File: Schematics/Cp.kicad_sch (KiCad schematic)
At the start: 60 parts, among them Q10 J201, Q11 J201, Q3 2SC1815, Q4 2SC1815, Q5 2SC1815, Q6 2SC1815, Q7 2SC1815, Q8 2SC1815, Q9 2SC1815, SW1 SW_SPDT, U1 CA3080

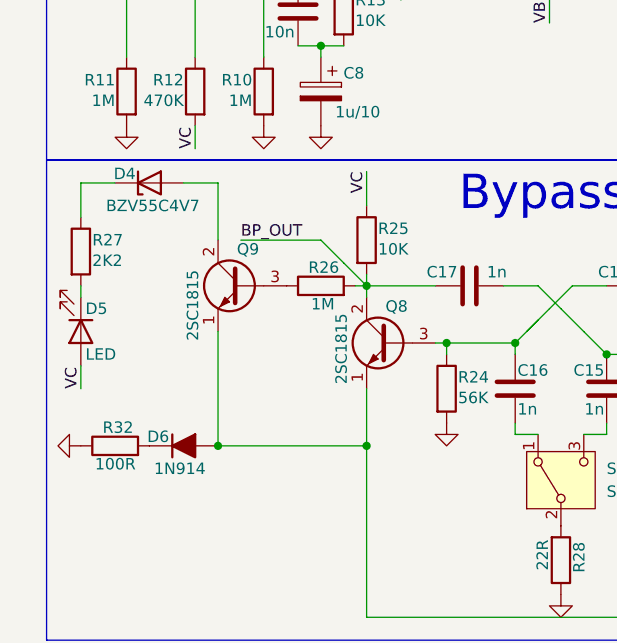
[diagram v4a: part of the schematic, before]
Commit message: Schem upd
The LED is powered by the low voltage supply, not by the effect
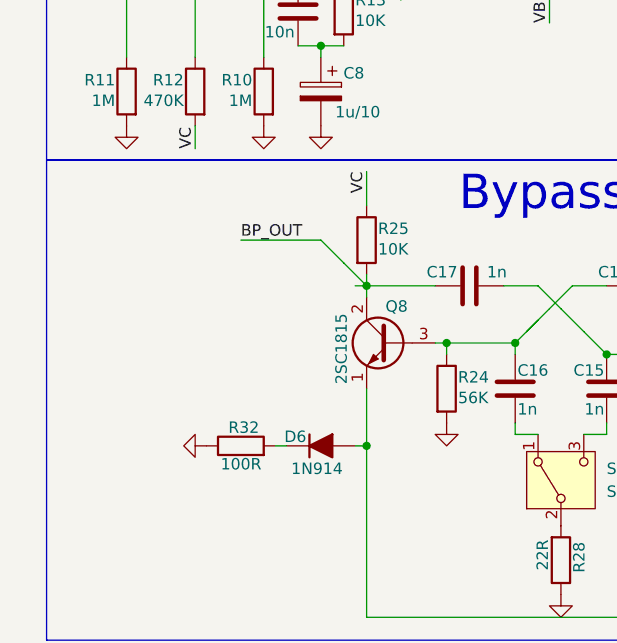
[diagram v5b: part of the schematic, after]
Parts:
- removed D4: BZV55C4V7, Diode_SMD:D_MiniMELF, symbol Diode:BZV55C4V7
- removed D5: LED, LED_THT:LED_BL-FL7680RGB, symbol Device:LED
- removed Q9: 2SC1815, Package_TO_SOT_THT:TO-92_Inline, symbol Transistor_BJT:2SC1815
- removed R26: 1M, Resistor_THT:R_Axial_DIN0207_L6.3mm_D2.5mm_P10.16mm_Horizontal, symbol Device:R
- removed R27: 2K2, Resistor_THT:R_Axial_DIN0207_L6.3mm_D2.5mm_P10.16mm_Horizontal, symbol Device:R
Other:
- moved on the sheet: D6, R32

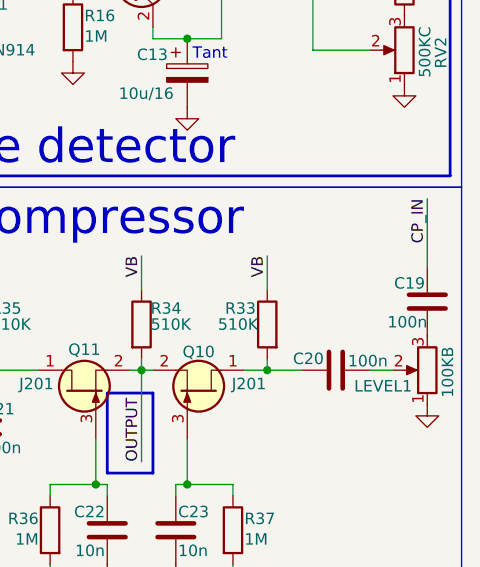
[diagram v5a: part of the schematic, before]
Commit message: Schem upd
Managed power supply for TL072
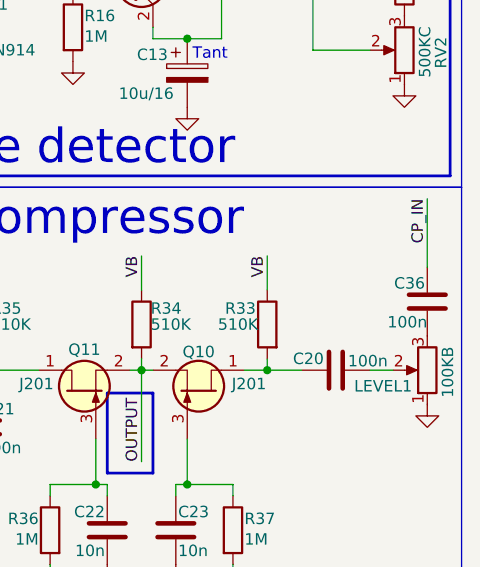
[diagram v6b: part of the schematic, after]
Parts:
- renumbered C19 to C36
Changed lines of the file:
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@@
 		(in_pos_files yes)
 		(dnp no)
-		(property "Reference" "C19"
+		(property "Reference" "C36"
 			(at 162.306 79.248 0)
 			(show_name no)
@@
 			(project "AMP-MA"
 				(path "/4094031b-a9da-4ac5-aaa1-42b342c92a3e/d432553b-ab0c-45ec-bbdd-5af2e9267855"
-					(reference "C19")
+					(reference "C36")
 					(unit 1)
 				)

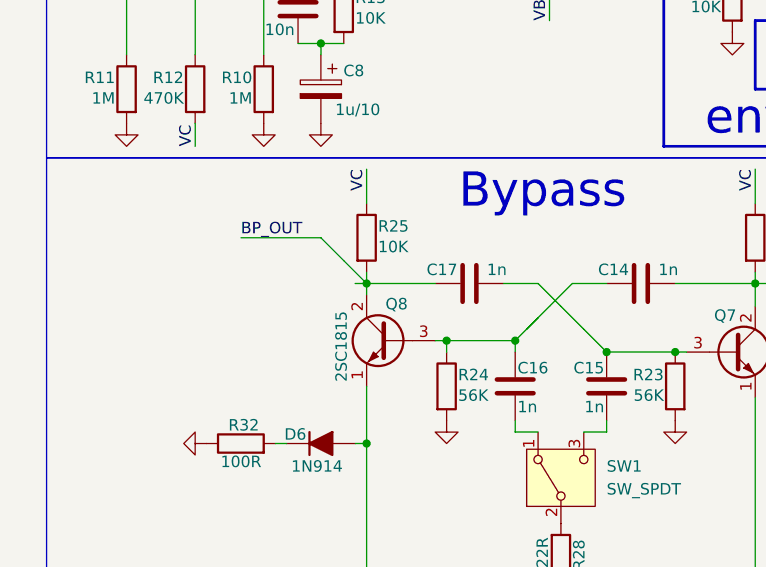
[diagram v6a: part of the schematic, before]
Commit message: Lib & Schematic upd
Jack connector symbol update. Made basic layout has been made
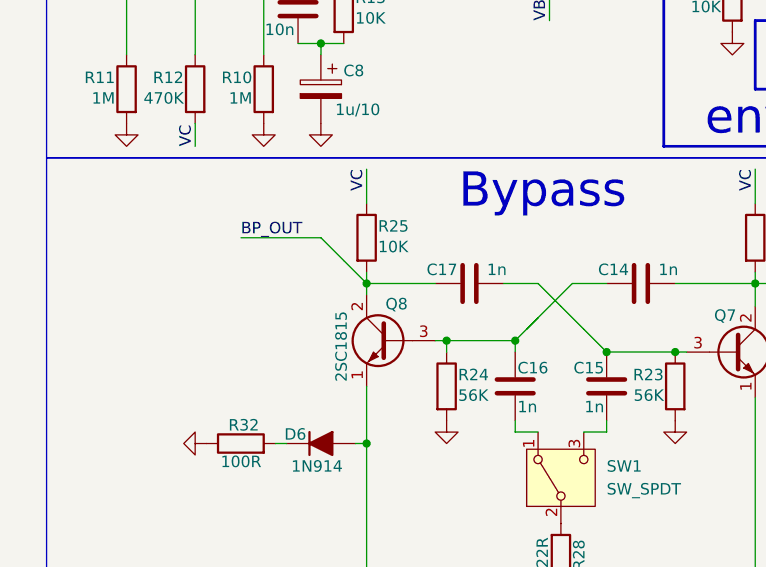
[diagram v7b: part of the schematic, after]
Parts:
- LEVEL1: footprint Potentiometer_SMD:Potentiometer_ACP_CA9-VSMD_Vertical_Hole -> Potentiometer_THT:Potentiometer_Alps_RK09Y11_Single_Horizontal
- RV1: footprint Potentiometer_THT:Potentiometer_Vishay_248BH-249BH_Single_Horizontal -> Potentiometer_THT:Potentiometer_ACP_CA9-H2,5_Horizontal
- RV2: footprint Potentiometer_SMD:Potentiometer_ACP_CA9-VSMD_Vertical_Hole -> Potentiometer_THT:Potentiometer_ACP_CA9-H2,5_Horizontal
- SW1: footprint Button_Switch_SMD:SW_SPDT_CK_JS102011SAQN -> Button_Switch_THT:SW_CK_JS202011AQN_DPDT_Angled
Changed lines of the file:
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@@
 	(wire
 		(pts
-			(xy 54.61 82.55) (xy 55.88 82.55)
-		)
-		(stroke
-			(width 0)
-			(type default)
-		)
-	)
-	(wire
-		(pts
 			(xy 72.39 99.06) (xy 74.93 99.06)
 		)
@@
 			)
 		)
-		(property "Footprint" "Potentiometer_THT:Potentiometer_Vishay_248BH-249BH_Single_Horizontal"
+		(property "Footprint" "Potentiometer_THT:Potentiometer_ACP_CA9-H2,5_Horizontal"
 			(at 36.83 40.64 0)
 			(hide yes)
@@
 			)
 		)
-		(property "Footprint" "Potentiometer_SMD:Potentiometer_ACP_CA9-VSMD_Vertical_Hole"
+		(property "Footprint" "Potentiometer_THT:Potentiometer_ACP_CA9-H2,5_Horizontal"
 			(at 160.02 53.34 0)
 			(hide yes)
@@
 			)
 		)
-		(property "Footprint" "Potentiometer_SMD:Potentiometer_ACP_CA9-VSMD_Vertical_Hole"
+		(property "Footprint" "Potentiometer_THT:Potentiometer_Alps_RK09Y11_Single_Horizontal"
 			(at 162.56 88.9 0)
 			(hide yes)
@@
 			)
 		)
-		(property "Footprint" "Button_Switch_SMD:SW_SPDT_CK_JS102011SAQN"
+		(property "Footprint" "Button_Switch_THT:SW_CK_JS202011AQN_DPDT_Angled"
 			(at 77.47 104.14 0)
 			(hide yes)

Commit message: smal schem upd
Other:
- moved on the sheet: C14, C15, C16, C17, C20, C21, C22, C23, C36, D6, LEVEL1, Q10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
